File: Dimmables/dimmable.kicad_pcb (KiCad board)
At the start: 2 copper layers, 55.9 x 84 mm, 8 parts, among them P1 LED, P2 MISC, Q1 IRF540N, U1 LM7805CT, U2 PHOTON

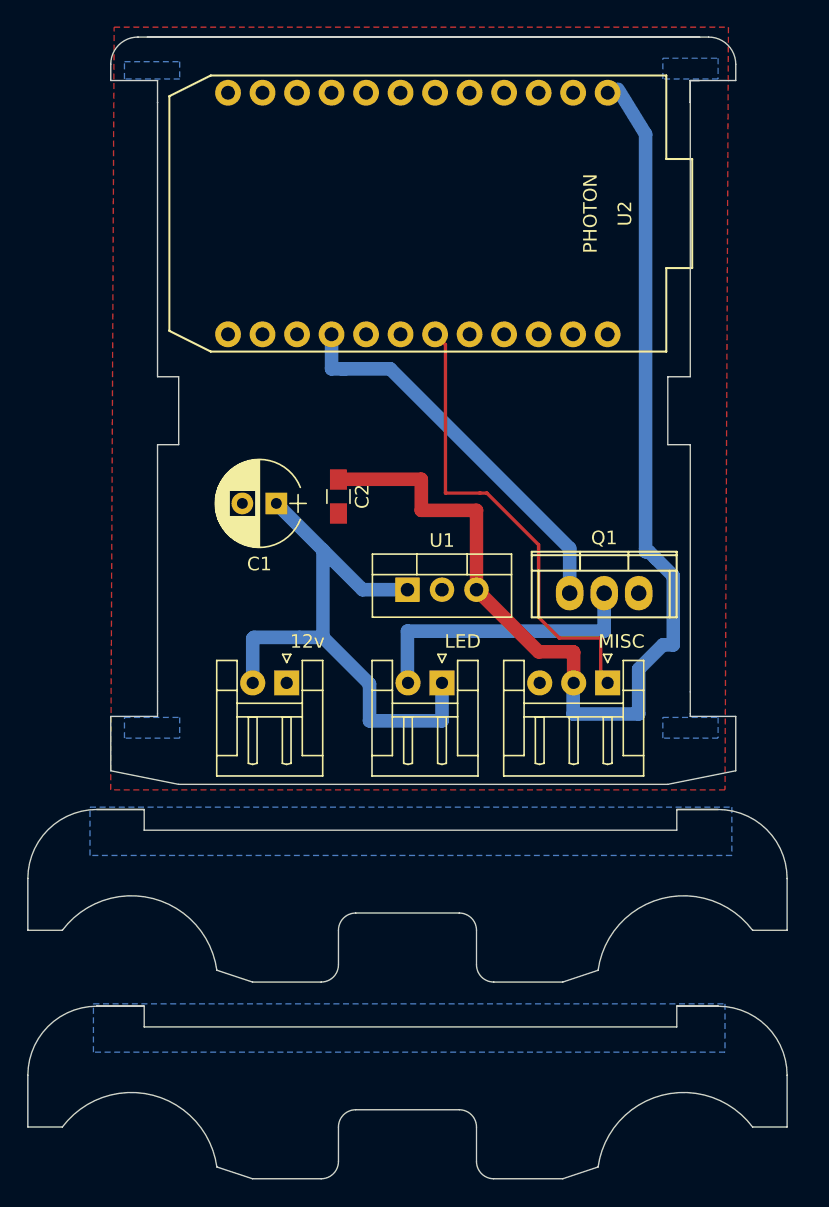
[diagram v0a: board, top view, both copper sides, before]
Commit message: production files for wifi dimmer, visual changes
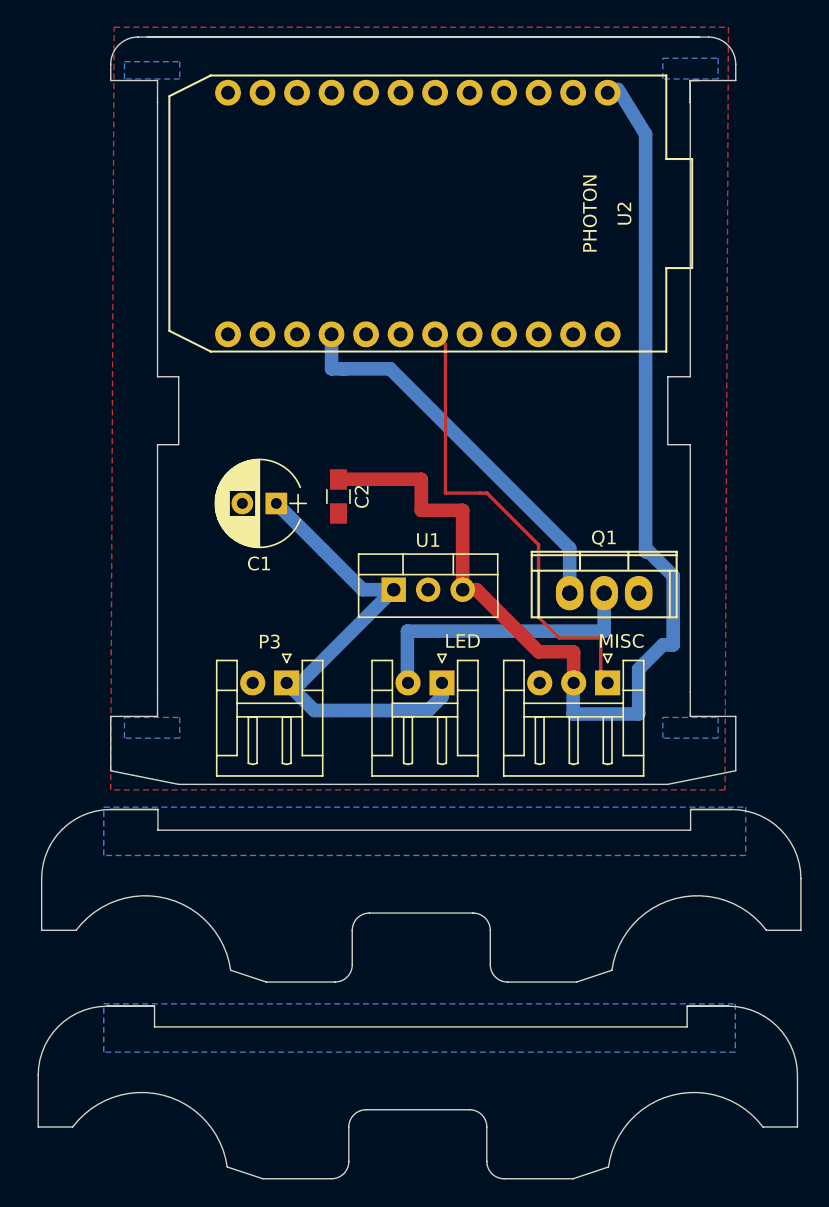
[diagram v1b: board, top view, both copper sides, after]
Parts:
- removed 12V: 12v, Connectors_JST:JST_EH_S02B-EH_02x2.50mm_Angled
- added P3: CONN_01X02, Connectors_JST:JST_EH_S02B-EH_02x2.50mm_Angled, F.Cu at (171.4, 97.5)
- moved U1 1.02 mm to (179.3, 90.7)
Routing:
- net +12V: track 43.2 -> 35.7 mm
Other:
- board size 55.9 x 84 mm -> 56.1 x 84 mm
